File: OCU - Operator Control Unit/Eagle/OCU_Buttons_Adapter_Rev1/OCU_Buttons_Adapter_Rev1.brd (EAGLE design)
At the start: 32 x 69.7 mm, 12 parts, among them J1 1053091202, J2 1053091202, J3 1053091202, J4 1053091202, J5 505567-0271, J6 505567-0271, J7 505567-0371

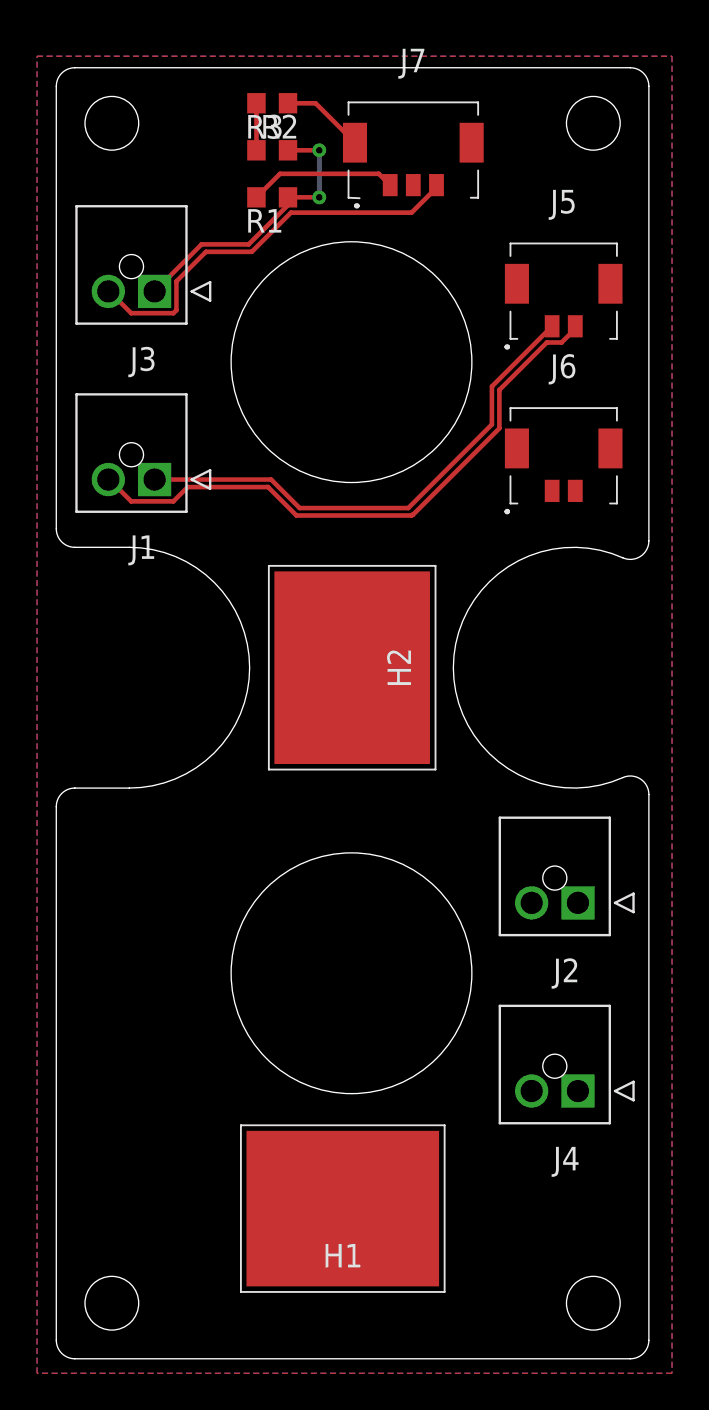
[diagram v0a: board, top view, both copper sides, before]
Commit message: finished button adapter, started with power pcb
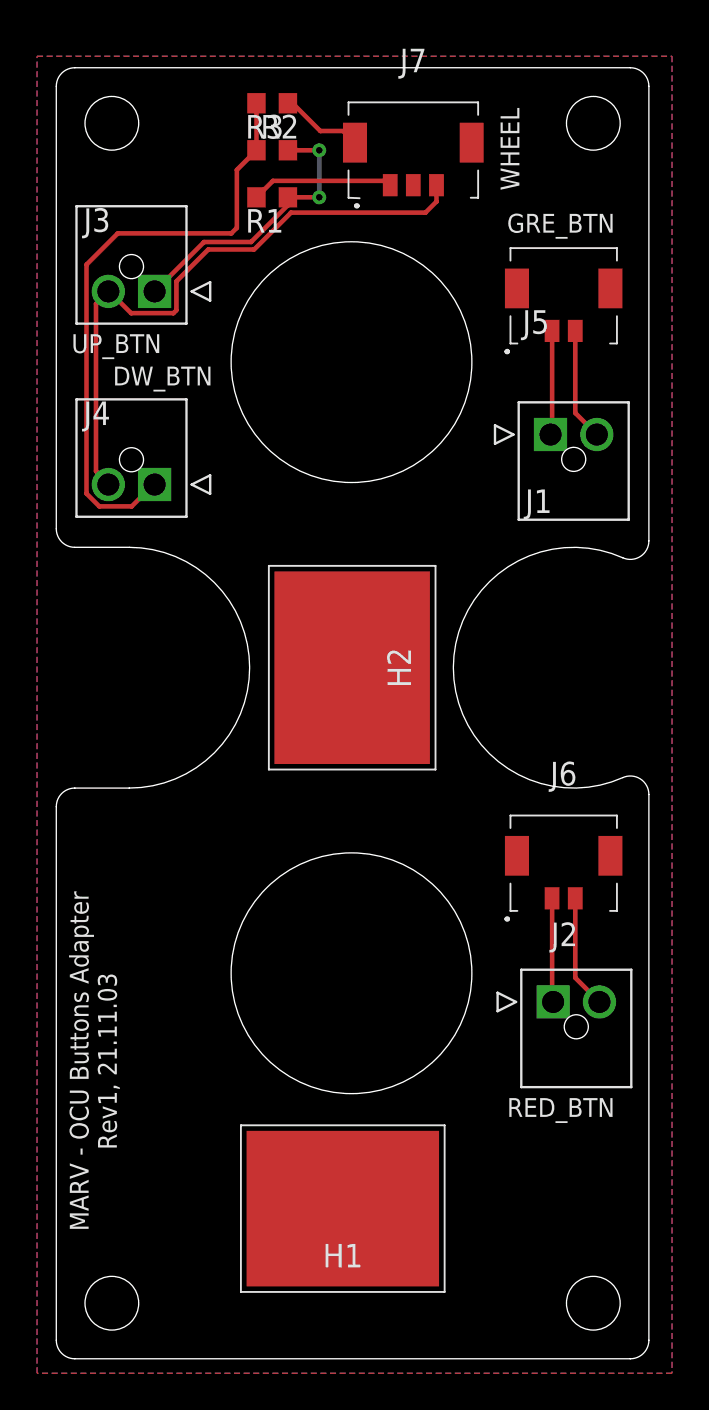
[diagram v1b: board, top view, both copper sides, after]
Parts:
- moved J4 39.9 mm to (-59.7, 9.89)
- moved J6 22.0 mm to (-37.6, -10.6)
- moved J1 21.5 mm to (-38.3, 12.6), turned to 0 degrees
- moved J2 5.52 mm to (-38.2, -18.1), turned to 0 degrees
- moved J5 0.25 mm to (-37.6, 20.1)
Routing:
- net N$6: track 2.54 -> 32.9 mm
- net N$2: track 32.2 -> 6.08 mm
- net N$1: track 27.4 -> 5.63 mm
- net N$7: track 22.1 -> 33.5 mm
- net N$4: track 0.00 -> 6.14 mm
- net N$3: track 0.00 -> 5.62 mm
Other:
- board text added: "DW_BTN"
- board text added: "GRE_BTN"
- board text added: "MARV - OCU Buttons Adapter Rev1, 21.11.03"
- board text added: "RED_BTN"
- board text added: "UP_BTN"
- board text added: "WHEEL"

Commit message: finished board
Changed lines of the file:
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@@
 <text x="-59.25" y="15.75" size="1.016" layer="21" ratio="10" align="center">DW_BTN</text>
 <text x="-40.5" y="28" size="1.016" layer="21" ratio="10" rot="R90" align="center">WHEEL</text>
-<text x="-63" y="-21.25" size="1.016" layer="21" ratio="10" rot="R90" align="center">MARV - OCU Buttons Adapter
+<text x="-62" y="-21.25" size="1.016" layer="21" ratio="10" rot="R90" align="center">MARV - OCU Buttons Adapter
 Rev1, 21.11.03</text>
 </plain>
